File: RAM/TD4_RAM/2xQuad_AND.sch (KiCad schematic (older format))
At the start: 2 parts, among them U4 74HC21

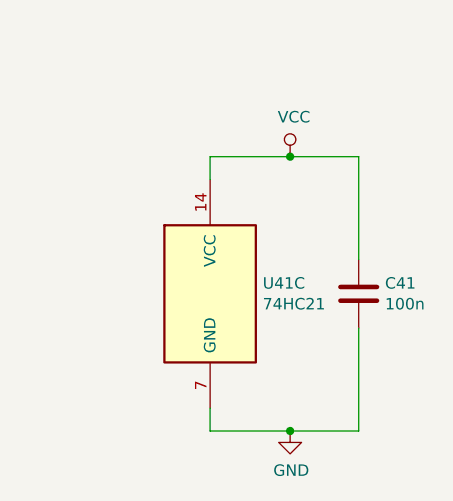
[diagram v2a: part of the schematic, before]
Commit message: Main RAM blocks routed
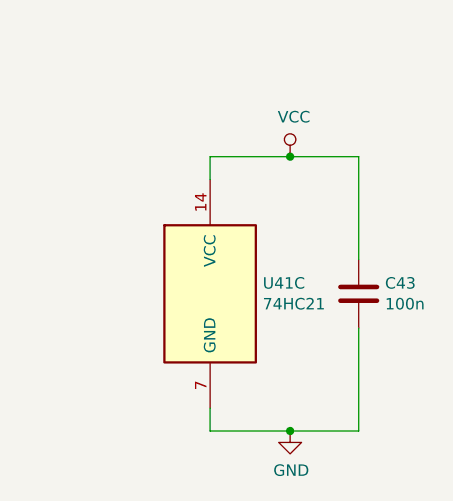
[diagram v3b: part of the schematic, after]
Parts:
- renumbered C4 to C6
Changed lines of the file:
@@
 $EndComp
 $Comp
-L Device:C C4
+L Device:C C6
 U 1 1 5C84DA33
 P 8700 5500
-AR Path="/5C5DC05E/5C84D72F/5C84DA33" Ref="C4"  Part="1"
+AR Path="/5C5DC05E/5C84D72F/5C84DA33" Ref="C6"  Part="1"
 AR Path="/5C5DC05E/5C8E8F76/5C84DA33" Ref="C?"  Part="1"
 AR Path="/5C5DC05E/5C8E8F7D/5C84DA33" Ref="C?"  Part="1"
@@
 AR Path="/5C5DC05E/5C8E8FAE/5C84DA33" Ref="C?"  Part="1"
 AR Path="/5C5DC05E/5C8E8FB4/5C84DA33" Ref="C?"  Part="1"
-AR Path="/5C5DC05E/5CD2847D/5C84DA33" Ref="C35"  Part="1"
-AR Path="/5C5DC05E/5CD2F166/5C84DA33" Ref="C36"  Part="1"
-AR Path="/5C5DC05E/5CD35E4F/5C84DA33" Ref="C37"  Part="1"
-AR Path="/5C5DC05E/5CD3CB4F/5C84DA33" Ref="C38"  Part="1"
-AR Path="/5C5DC05E/5CD3CB55/5C84DA33" Ref="C39"  Part="1"
-AR Path="/5C5DC05E/5CD3CB5B/5C84DA33" Ref="C40"  Part="1"
-AR Path="/5C5DC05E/5CD3CB61/5C84DA33" Ref="C41"  Part="1"
-F 0 "C41" H 8815 5546 50  0000 L CNN
+AR Path="/5C5DC05E/5CD2847D/5C84DA33" Ref="C37"  Part="1"
+AR Path="/5C5DC05E/5CD2F166/5C84DA33" Ref="C38"  Part="1"
+AR Path="/5C5DC05E/5CD35E4F/5C84DA33" Ref="C39"  Part="1"
+AR Path="/5C5DC05E/5CD3CB4F/5C84DA33" Ref="C40"  Part="1"
+AR Path="/5C5DC05E/5CD3CB55/5C84DA33" Ref="C41"  Part="1"
+AR Path="/5C5DC05E/5CD3CB5B/5C84DA33" Ref="C42"  Part="1"
+AR Path="/5C5DC05E/5CD3CB61/5C84DA33" Ref="C43"  Part="1"
+F 0 "C43" H 8815 5546 50  0000 L CNN
 F 1 "100n" H 8815 5455 50  0000 L CNN
 F 2 "Capacitor_SMD:C_0805_2012Metric" H 8738 5350 50  0001 C CNN
@@
 	8700 5650 8700 6100
 $Comp
-L power:GND #PWR025
+L power:GND #PWR030
 U 1 1 5C84DB98
 P 8400 6100
-AR Path="/5C5DC05E/5C84D72F/5C84DB98" Ref="#PWR025"  Part="1"
+AR Path="/5C5DC05E/5C84D72F/5C84DB98" Ref="#PWR030"  Part="1"
 AR Path="/5C5DC05E/5C8E8F76/5C84DB98" Ref="#PWR?"  Part="1"
 AR Path="/5C5DC05E/5C8E8F7D/5C84DB98" Ref="#PWR?"  Part="1"
@@
 AR Path="/5C5DC05E/5C8E8FAE/5C84DB98" Ref="#PWR?"  Part="1"
 AR Path="/5C5DC05E/5C8E8FB4/5C84DB98" Ref="#PWR?"  Part="1"
-AR Path="/5C5DC05E/5CD2847D/5C84DB98" Ref="#PWR0147"  Part="1"
-AR Path="/5C5DC05E/5CD2F166/5C84DB98" Ref="#PWR0149"  Part="1"
-AR Path="/5C5DC05E/5CD35E4F/5C84DB98" Ref="#PWR0151"  Part="1"
-AR Path="/5C5DC05E/5CD3CB4F/5C84DB98" Ref="#PWR0153"  Part="1"
-AR Path="/5C5DC05E/5CD3CB55/5C84DB98" Ref="#PWR0155"  Part="1"
-AR Path="/5C5DC05E/5CD3CB5B/5C84DB98" Ref="#PWR0157"  Part="1"
-AR Path="/5C5DC05E/5CD3CB61/5C84DB98" Ref="#PWR0159"  Part="1"
-F 0 "#PWR0159" H 8400 5850 50  0001 C CNN
+AR Path="/5C5DC05E/5CD2847D/5C84DB98" Ref="#PWR0152"  Part="1"
+AR Path="/5C5DC05E/5CD2F166/5C84DB98" Ref="#PWR0154"  Part="1"
+AR Path="/5C5DC05E/5CD35E4F/5C84DB98" Ref="#PWR0156"  Part="1"
+AR Path="/5C5DC05E/5CD3CB4F/5C84DB98" Ref="#PWR0158"  Part="1"
+AR Path="/5C5DC05E/5CD3CB55/5C84DB98" Ref="#PWR0160"  Part="1"
+AR Path="/5C5DC05E/5CD3CB5B/5C84DB98" Ref="#PWR0162"  Part="1"
+AR Path="/5C5DC05E/5CD3CB61/5C84DB98" Ref="#PWR0164"  Part="1"
+F 0 "#PWR0164" H 8400 5850 50  0001 C CNN
 F 1 "GND" H 8405 5927 50  0000 C CNN
 F 2 "" H 8400 6100 50  0001 C CNN
@@
 	8400 6100 8700 6100
 $Comp
-L power:VCC #PWR024
+L power:VCC #PWR029
 U 1 1 5C84DC2A
 P 8400 4900
-AR Path="/5C5DC05E/5C84D72F/5C84DC2A" Ref="#PWR024"  Part="1"
+AR Path="/5C5DC05E/5C84D72F/5C84DC2A" Ref="#PWR029"  Part="1"
 AR Path="/5C5DC05E/5C8E8F76/5C84DC2A" Ref="#PWR?"  Part="1"
 AR Path="/5C5DC05E/5C8E8F7D/5C84DC2A" Ref="#PWR?"  Part="1"
@@
 AR Path="/5C5DC05E/5C8E8FAE/5C84DC2A" Ref="#PWR?"  Part="1"
 AR Path="/5C5DC05E/5C8E8FB4/5C84DC2A" Ref="#PWR?"  Part="1"
-AR Path="/5C5DC05E/5CD2847D/5C84DC2A" Ref="#PWR0146"  Part="1"
-AR Path="/5C5DC05E/5CD2F166/5C84DC2A" Ref="#PWR0148"  Part="1"
-AR Path="/5C5DC05E/5CD35E4F/5C84DC2A" Ref="#PWR0150"  Part="1"
-AR Path="/5C5DC05E/5CD3CB4F/5C84DC2A" Ref="#PWR0152"  Part="1"
-AR Path="/5C5DC05E/5CD3CB55/5C84DC2A" Ref="#PWR0154"  Part="1"
-AR Path="/5C5DC05E/5CD3CB5B/5C84DC2A" Ref="#PWR0156"  Part="1"
-AR Path="/5C5DC05E/5CD3CB61/5C84DC2A" Ref="#PWR0158"  Part="1"
-F 0 "#PWR0158" H 8400 4750 50  0001 C CNN
+AR Path="/5C5DC05E/5CD2847D/5C84DC2A" Ref="#PWR0151"  Part="1"
+AR Path="/5C5DC05E/5CD2F166/5C84DC2A" Ref="#PWR0153"  Part="1"
+AR Path="/5C5DC05E/5CD35E4F/5C84DC2A" Ref="#PWR0155"  Part="1"
+AR Path="/5C5DC05E/5CD3CB4F/5C84DC2A" Ref="#PWR0157"  Part="1"
+AR Path="/5C5DC05E/5CD3CB55/5C84DC2A" Ref="#PWR0159"  Part="1"
+AR Path="/5C5DC05E/5CD3CB5B/5C84DC2A" Ref="#PWR0161"  Part="1"
+AR Path="/5C5DC05E/5CD3CB61/5C84DC2A" Ref="#PWR0163"  Part="1"
+F 0 "#PWR0163" H 8400 4750 50  0001 C CNN
 F 1 "VCC" H 8417 5073 50  0000 C CNN
 F 2 "" H 8400 4900 50  0001 C CNN
